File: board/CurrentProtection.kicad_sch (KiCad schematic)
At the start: 26 parts, among them Q3 DMN3008SFG, Q4 DMN3008SFG, U10 ACS72981LLRATR-100U3, U2 LM5050MK-1_NOPB, U3 LM5050MK-1_NOPB

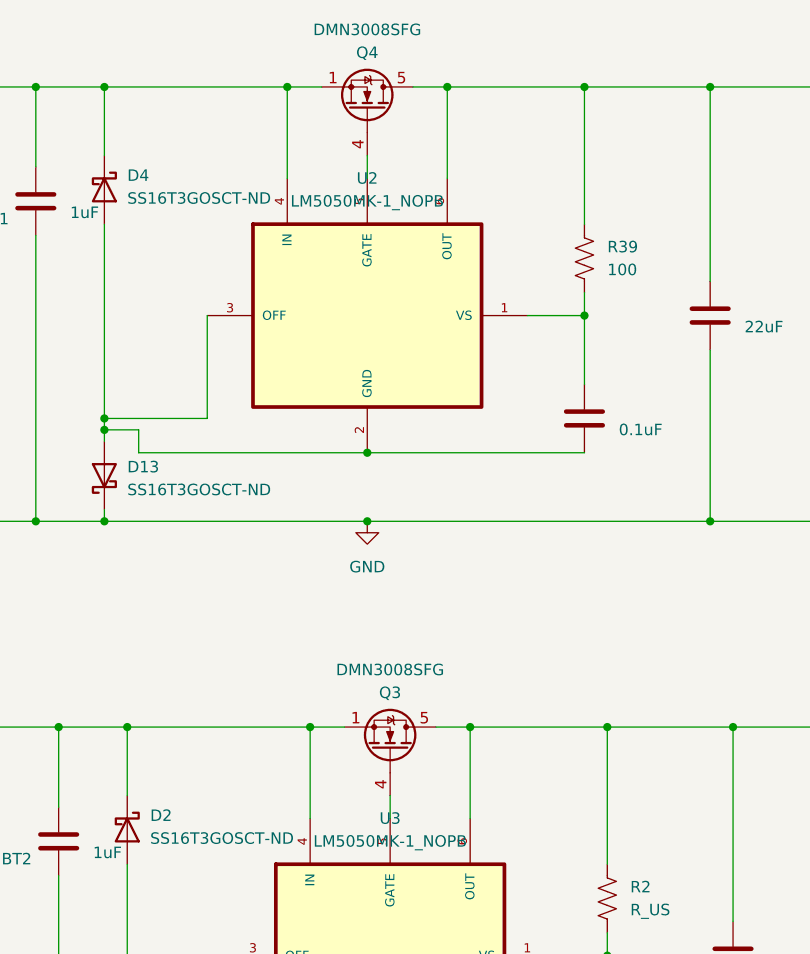
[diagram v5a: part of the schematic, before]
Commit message: add mosfett and teensy switch pins
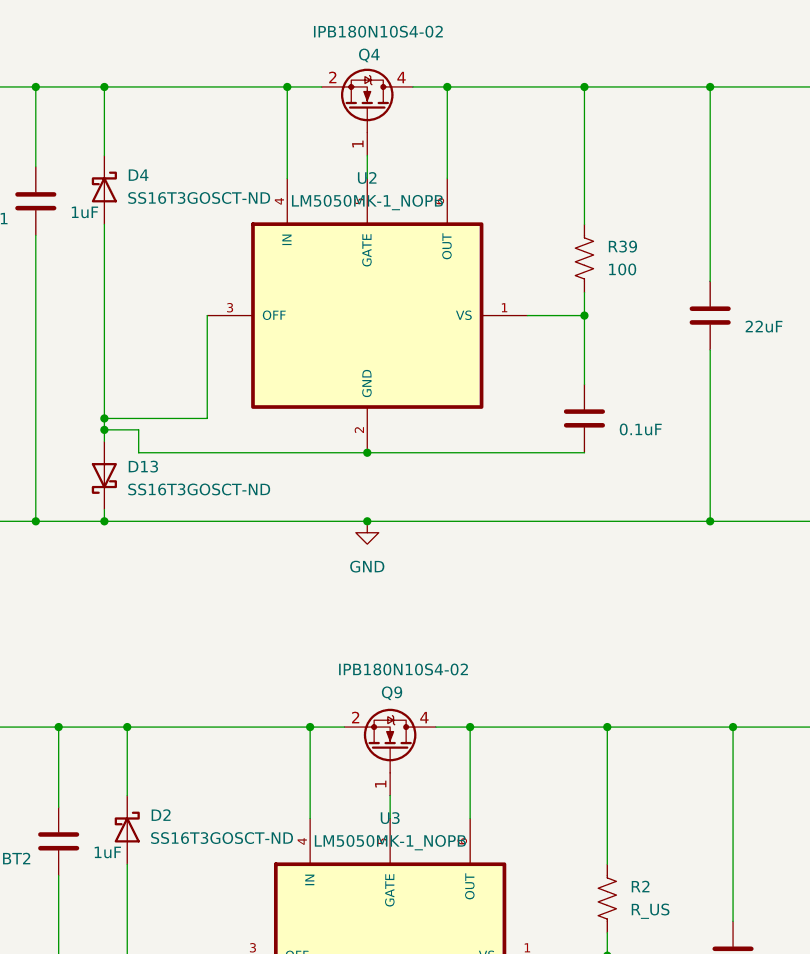
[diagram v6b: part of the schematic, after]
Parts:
- removed Q3, Q4: DMN3008SFG, Package_SON:Diodes_PowerDI3333-8, symbol Transistor_FET:DMN3008SFG
- added Q4, Q9: IPB180N10S4-02, Package_TO_SOT_SMD:TO-263-6, symbol Transistor_FET:IPB180N10S4-02
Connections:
- net at BT2.1 (+), C5.1, D2.1 (K)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: now also Q9.2 (S), Q9.3 (S), Q9.5 (S), Q9.6 (S), Q9.7 (S)
- net at BT1.1 (+), C11.1, D4.1 (K)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: now also Q4.2 (S), Q4.3 (S), Q4.5 (S), Q4.6 (S), Q4.7 (S)
- net at C13.1, C4.1, D14.1 (K)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: now also Q4.4 (D), Q9.4 (D)
- net at U3.5 (GATE): now also Q9.1 (G)
- net at U2.5 (GATE): now also Q4.1 (G)
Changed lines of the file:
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@@
+	)
+	(symbol
+		(lib_id "Transistor_FET:IPB180N10S4-02")
+		(at 81.28 147.32 270)
+		(mirror x)
+		(unit 1)
+		(exclude_from_sim no)
+		(in_bom yes)
+		(on_board yes)
+		(dnp no)
+		(property "Reference" "Q9"
+			(at 80.264 140.97 90)
+			(effects
+				(font
+					(size 1.27 1.27)
+				)
+				(justify left)
+			)
+		)
+		(property "Value" "IPB180N10S4-02"
+			(at 75.438 138.43 90)
+			(effects
+				(font
+					(size 1.27 1.27)
+				)
+				(justify left)
+			)
+		)
+		(property "Footprint" "Package_TO_SOT_SMD:TO-263-6"
+			(at 79.375 142.24 0)
+			(effects
+				(font
+					(size 1.27 1.27)
+					(italic yes)
+				)
+				(justify left)
+				(hide yes)
+			)
+		)
+		(property "Datasheet" "https://www.infineon.com/dgdl/Infineon-IPB180N10S4_02-DS-v01_00-en.pdf?fileId=db3a30433d1d0bbe013d2129cf8a2f88"
+			(at 77.47 142.24 0)
+			(effects
+				(font
+					(size 1.27 1.27)
+				)
+				(justify left)
+				(hide yes)
+			)
+		)
+		(property "Description" "180A Id, 100V Vds, OptiMOS-T2 N-Channel Power MOSFET, 2.5mOhm Ron, Qg (typ) 156nC, TO-263-6"
+			(at 81.28 147.32 0)
+			(effects
+				(font
+					(size 1.27 1.27)
+				)
+				(hide yes)
+			)
+		)
+		(pin "5"
+		)
+		(pin "3"
+		)
+		(pin "7"
+		)
+		(pin "2"
+		)
+		(pin "1"
+		)
+		(pin "4"
+		)
+		(pin "6"
+		)
+		(instances
+			(project "PowerManagementBoard"
+				(path "/7eaa639d-7062-45e7-be05-1c2855431307/fa17e088-8bc3-4875-b327-c5ed0adaa270"
+					(reference "Q9")
+					(unit 1)
+				)
+			)
+		)
 	)
 	(symbol
@@
 				(path "/7eaa639d-7062-45e7-be05-1c2855431307/fa17e088-8bc3-4875-b327-c5ed0adaa270"
 					(reference "#PWR02")
-					(unit 1)
-				)
-			)
-		)
-	)
-	(symbol
-		(lib_id "Transistor_FET:DMN3008SFG")
-		(at 81.28 147.32 270)
-		(mirror x)
-		(unit 1)
-		(exclude_from_sim no)
-		(in_bom yes)
-		(on_board yes)
-		(dnp no)
-		(property "Reference" "Q3"
-			(at 81.28 140.97 90)
-			(effects
-				(font
-					(size 1.27 1.27)
-				)
-			)
-		)
-		(property "Value" "DMN3008SFG"
-			(at 81.28 138.43 90)
-			(effects
-				(font
-					(size 1.27 1.27)
-				)
-			)
-		)
-		(property "Footprint" "Package_SON:Diodes_PowerDI3333-8"
-			(at 79.375 142.24 0)
-			(effects
-				(font
-					(size 1.27 1.27)
-					(italic yes)
-				)
-				(justify left)
-				(hide yes)
-			)
-		)
-		(property "Datasheet" "https://www.diodes.com/assets/Datasheets/DMN3008SFG.pdf"
-			(at 77.47 142.24 0)
-			(effects
-				(font
-					(size 1.27 1.27)
-				)
-				(justify left)
-				(hide yes)
-			)
-		)
-		(property "Description" "17.6A Id, 30V Vds, N-Channel Power MOSFET, 4.4mOhm Ron, 86nC Qg (typ), PowerDI3333-8"
-			(at 81.28 147.32 0)
-			(effects
-				(font
-					(size 1.27 1.27)
-				)
-				(hide yes)
-			)
-		)
-		(pin "5"
-		)
-		(pin "1"
-		)
-		(pin "4"
-		)
-		(pin "3"
-		)
-		(pin "2"
-		)
-		(instances
-			(project "PowerManagementBoard"
-				(path "/7eaa639d-7062-45e7-be05-1c2855431307/fa17e088-8bc3-4875-b327-c5ed0adaa270"
-					(reference "Q3")
 					(unit 1)
 				)
@@
 	)
 	(symbol
+		(lib_id "Transistor_FET:IPB180N10S4-02")
+		(at 78.74 76.2 270)
+		(mirror x)
+		(unit 1)
+		(exclude_from_sim no)
+		(in_bom yes)
+		(on_board yes)
+		(dnp no)
+		(property "Reference" "Q4"
+			(at 77.724 70.104 90)
+			(effects
+				(font
+					(size 1.27 1.27)
+				)
+				(justify left)
+			)
+		)
+		(property "Value" "IPB180N10S4-02"
+			(at 72.644 67.564 90)
+			(effects
+				(font
+					(size 1.27 1.27)
+				)
+				(justify left)
+			)
+		)
+		(property "Footprint" "Package_TO_SOT_SMD:TO-263-6"
+			(at 76.835 71.12 0)
+			(effects
+				(font
+					(size 1.27 1.27)
+					(italic yes)
+				)
+				(justify left)
+				(hide yes)
+			)
+		)
+		(property "Datasheet" "https://www.infineon.com/dgdl/Infineon-IPB180N10S4_02-DS-v01_00-en.pdf?fileId=db3a30433d1d0bbe013d2129cf8a2f88"
+			(at 74.93 71.12 0)
+			(effects
+				(font
+					(size 1.27 1.27)
+				)
+				(justify left)
+				(hide yes)
+			)
+		)
+		(property "Description" "180A Id, 100V Vds, OptiMOS-T2 N-Channel Power MOSFET, 2.5mOhm Ron, Qg (typ) 156nC, TO-263-6"
+			(at 78.74 76.2 0)
+			(effects
+				(font
+					(size 1.27 1.27)
+				)
+				(hide yes)
+			)
+		)
+		(pin "5"
+		)
+		(pin "3"
+		)
+		(pin "7"
+		)
+		(pin "2"
+		)
+		(pin "1"
+		)
+		(pin "4"
+		)
+		(pin "6"
+		)
+		(instances
+			(project "PowerManagementBoard"
+				(path "/7eaa639d-7062-45e7-be05-1c2855431307/fa17e088-8bc3-4875-b327-c5ed0adaa270"
+					(reference "Q4")
+					(unit 1)
+				)
+			)
+		)
+	)
+	(symbol
 		(lib_id "Device:C")
 		(at 119.38 170.18 0)
@@
 					(unit 1)
 				)
-			)
-		)
-	)
-	(symbol
-		(lib_id "Transistor_FET:DMN3008SFG")
-		(at 78.74 76.2 270)
-		(mirror x)
-		(unit 1)
-		(exclude_from_sim no)
-		(in_bom yes)
-		(on_board yes)
-		(dnp no)
-		(property "Reference" "Q4"
-			(at 78.74 69.85 90)
-			(effects
-				(font
-					(size 1.27 1.27)
-				)
-			)
-		)
-		(property "Value" "DMN3008SFG"
-			(at 78.74 67.31 90)
-			(effects
-				(font
-					(size 1.27 1.27)
-				)
-			)
-		)
-		(property "Footprint" "Package_SON:Diodes_PowerDI3333-8"
-			(at 76.835 71.12 0)
-			(effects
-				(font
-					(size 1.27 1.27)
-					(italic yes)
-				)
-				(justify left)
-				(hide yes)
-			)
-		)
-		(property "Datasheet" "https://www.diodes.com/assets/Datasheets/DMN3008SFG.pdf"
-			(at 74.93 71.12 0)
-			(effects
-				(font
-					(size 1.27 1.27)
-				)
-				(justify left)
-				(hide yes)
-			)
-		)
-		(property "Description" "17.6A Id, 30V Vds, N-Channel Power MOSFET, 4.4mOhm Ron, 86nC Qg (typ), PowerDI3333-8"
-			(at 78.74 76.2 0)
-			(effects
-				(font
-					(size 1.27 1.27)
-				)
-				(hide yes)
-			)
-		)
-		(pin "5"
-		)
-		(pin "1"
-		)
-		(pin "4"
-		)
-		(pin "3"
-		)
-		(pin "2"
-		)
-		(instances
-			(project "PowerManagementBoard"
-				(path "/7eaa639d-7062-45e7-be05-1c2855431307/fa17e088-8bc3-4875-b327-c5ed0adaa270"
-					(reference "Q4")
-					(unit 1)
-				)

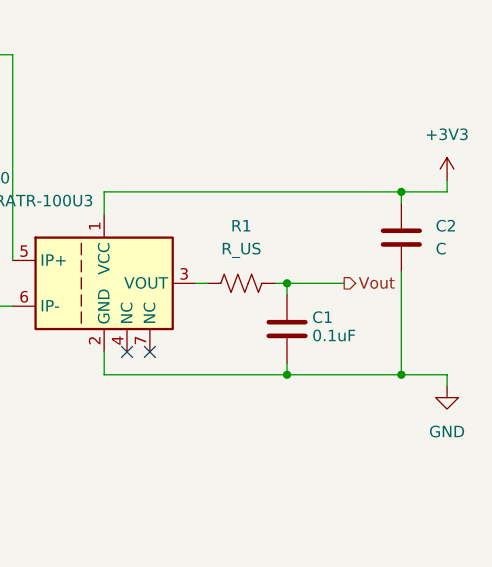
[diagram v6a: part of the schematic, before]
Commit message: BattCSense added
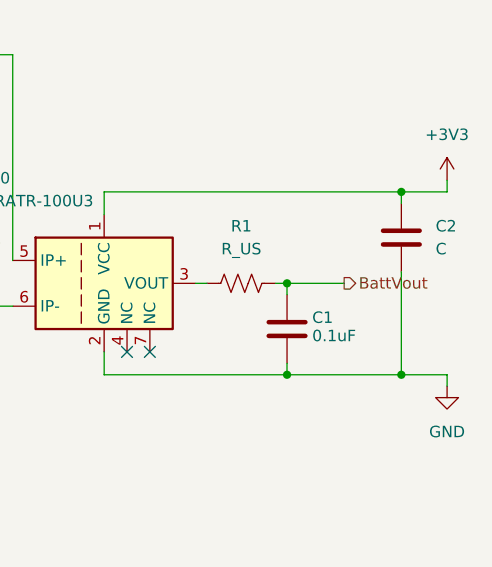
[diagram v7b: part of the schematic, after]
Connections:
- net Vout renamed BattVout
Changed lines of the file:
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@@
 		)
 	)
-	(hierarchical_label "Vout"
+	(hierarchical_label "BattVout"
 		(shape output)
 		(at 207.01 99.06 0)

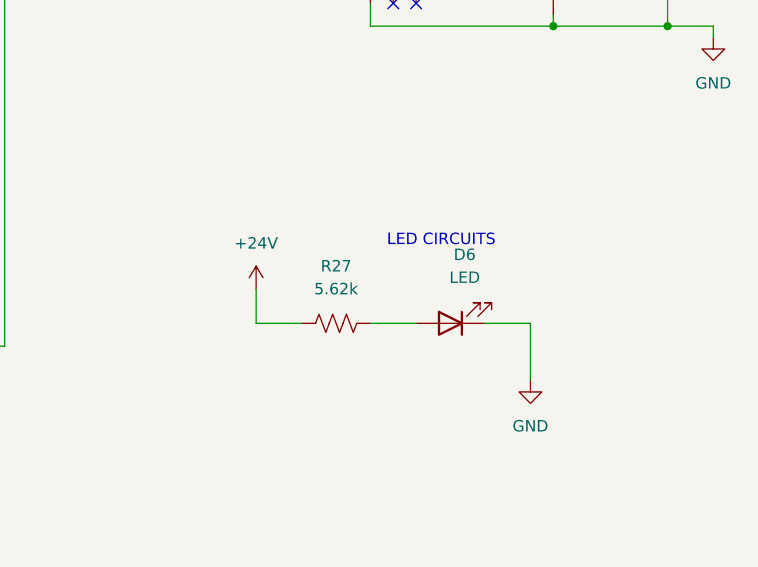
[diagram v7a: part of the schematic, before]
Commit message: added power leds
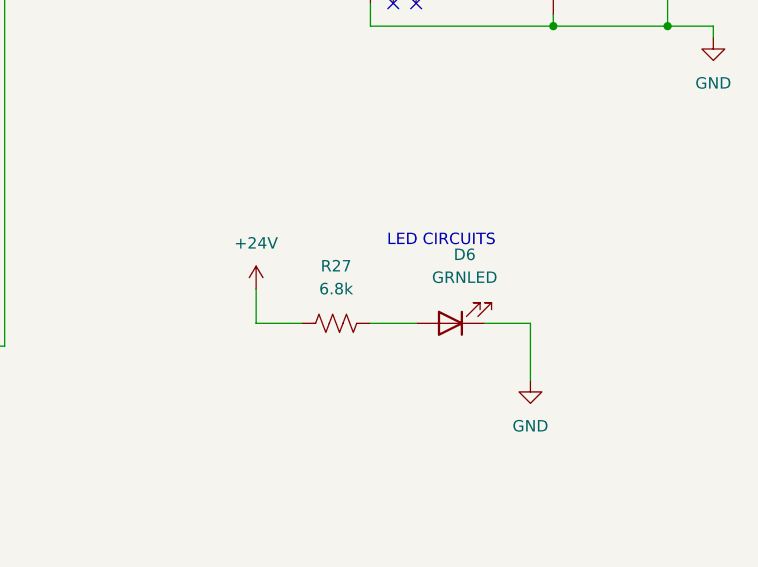
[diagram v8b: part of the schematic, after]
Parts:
- D6: value LED -> GRNLED
- R27: value 5.62k -> 6.8k
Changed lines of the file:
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@@
 			)
 		)
-		(property "Value" "LED"
+		(property "Value" "GRNLED"
 			(at 190.8175 137.16 0)
 			(effects
@@
 			)
 		)
-		(property "Value" "5.62k"
+		(property "Value" "6.8k"
 			(at 176.53 138.43 90)
 			(effects
